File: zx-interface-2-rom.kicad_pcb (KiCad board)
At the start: 4 copper layers, 39.4 x 50.1 mm, 9 parts, among them J1 cartridge_IF2, SW1 SW_DIP_x02, U1 W27C512, U2 74LS32

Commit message: Updated SYMBOL & FOOTPRINT library
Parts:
- G200: footprint ZXINFO_LIB:ZXInfo_kicad_logo_copper_16.5x5 -> ZXINFO_FOOTPRINT:ZXInfo_kicad_logo_copper_16.5x5
- J1: footprint ZXINFO_LIB:CART_IF2_EDGE -> ZXINFO_FOOTPRINT:CART_IF2_EDGE; moved to F.Cu
- moved U1 36.5 mm to (87.1, 80.7), turned to 90 degrees
- moved J1 31.7 mm to (79.5, 90.4), turned to 0 degrees
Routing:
- net +5V: track 95.1 -> 0.00 mm
- net Net-(J1-A15): track 51.0 -> 0.00 mm
- net Net-(U1-A15): track 42.9 -> 0.00 mm
- net Net-(J1-~{MREQ}): track 41.8 -> 0.00 mm
- net Net-(J1-A14): track 37.8 -> 0.00 mm
- net Net-(U1-A14): track 37.0 -> 0.00 mm
- net A4: track 29.1 -> 0.00 mm, vias 1 -> 0
- net A5: track 29.0 -> 0.00 mm, vias 1 -> 0
- net A0: track 28.8 -> 0.00 mm, vias 1 -> 0
- net A1: track 28.8 -> 0.00 mm, vias 1 -> 0
- net A3: track 28.3 -> 0.00 mm, vias 1 -> 0
- net A2: track 28.0 -> 0.00 mm, vias 1 -> 0
- net D1: track 27.6 -> 0.00 mm
- net D2: track 27.6 -> 0.00 mm
- net D0: track 27.6 -> 0.00 mm
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- removed copper zone on B.Cu, net GND

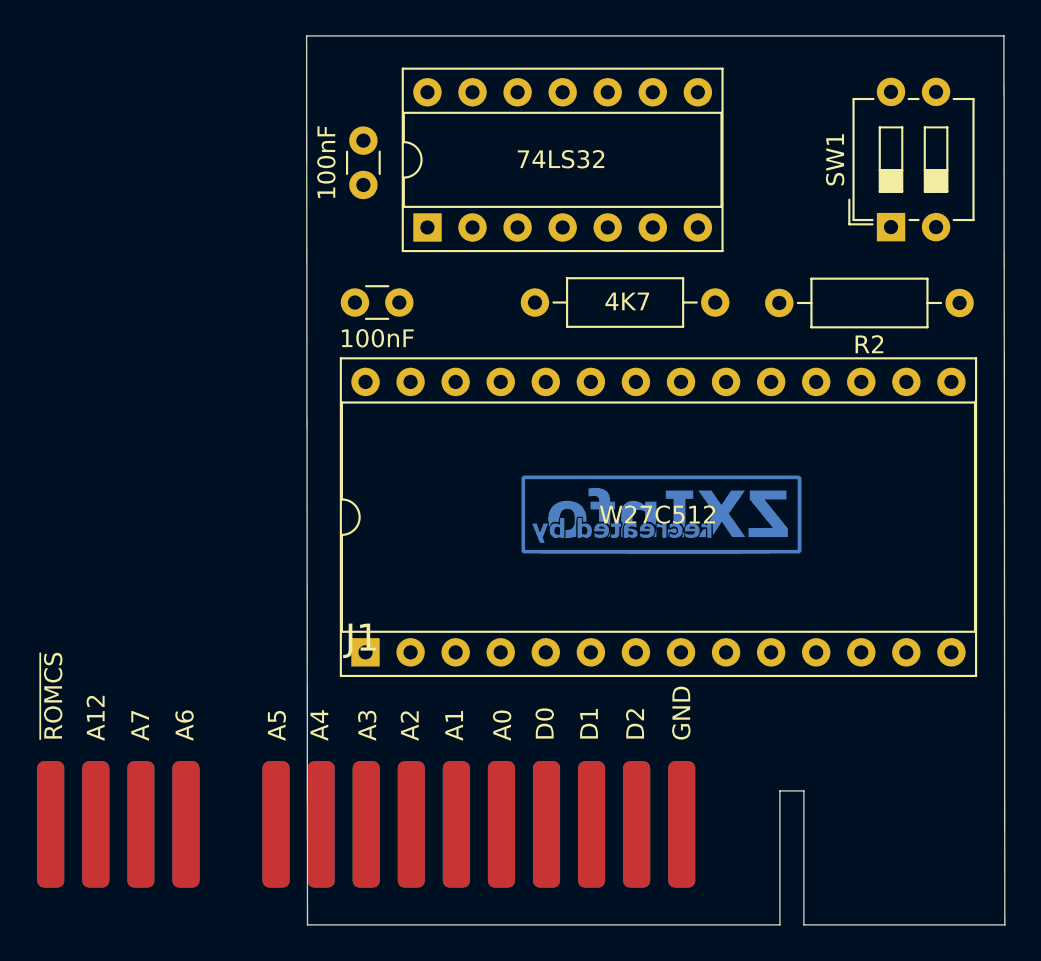
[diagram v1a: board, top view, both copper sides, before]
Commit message: version 2 - added solder mask to pad
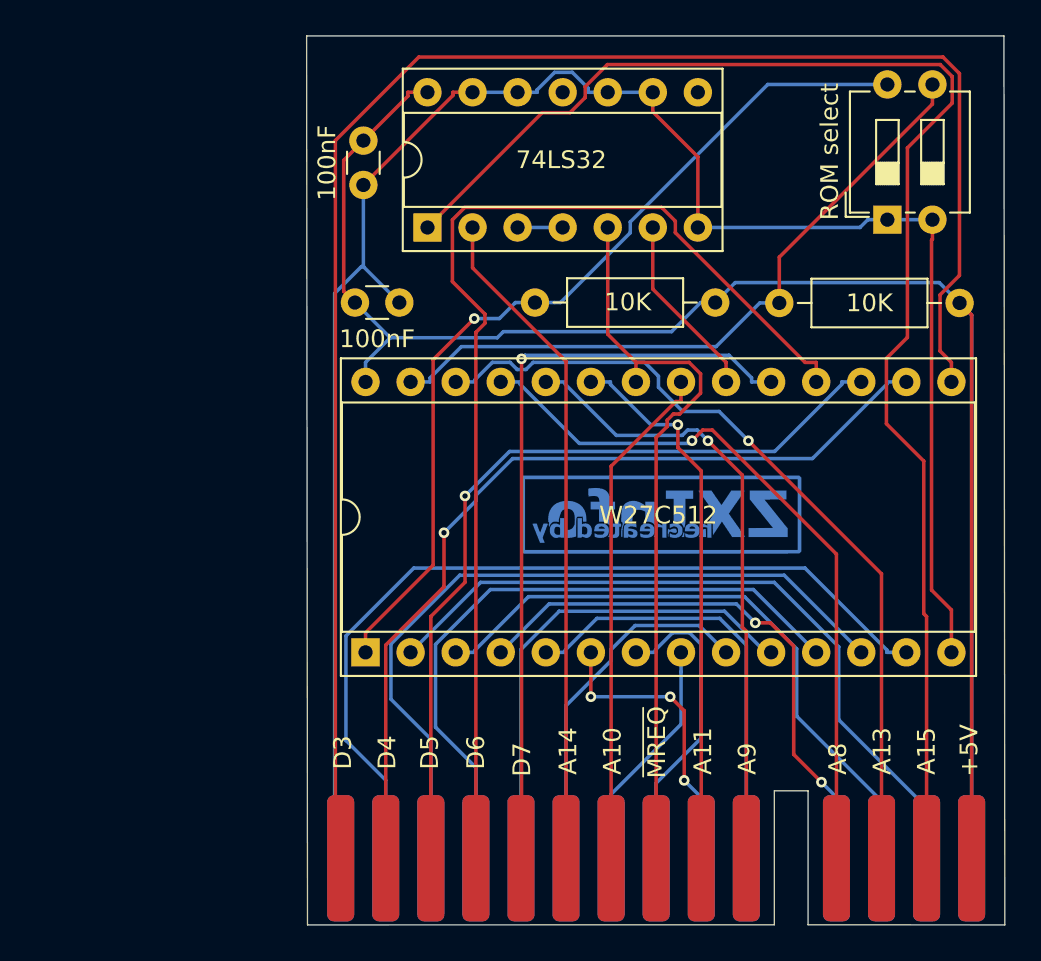
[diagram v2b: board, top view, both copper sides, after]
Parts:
- J1: moved to B.Cu
- R1, R2: value 4K7 -> 10K
- SW1: value SW_DIP_x02 -> ROM select
- moved J1 31.6 mm to (111.1, 92.3), turned to 180 degrees
- moved SW1 0.47 mm to (116.5, 56.3)
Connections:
- SW1 pad 3: Net-(U1-A15) -> Net-(U1-A14)
- SW1 pad 4: Net-(U1-A14) -> Net-(U1-A15)
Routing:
- net +5V: track 0.00 -> 117.6 mm
- net GND: track 0.00 -> 108.4 mm
- net D3: track 0.00 -> 96.2 mm
- net Net-(J1-A15): track 0.00 -> 80.5 mm
- net D6: track 0.00 -> 62.8 mm
- net Net-(U1-A15): track 0.00 -> 50.5 mm, vias 0 -> 1
- net D4: track 0.00 -> 49.5 mm, vias 0 -> 1
- net D2: track 0.00 -> 48.7 mm
- net D5: track 0.00 -> 46.3 mm, vias 0 -> 1
- net A13: track 0.00 -> 46.2 mm, vias 0 -> 1
- net D7: track 0.00 -> 43.1 mm, vias 0 -> 1
- net D1: track 0.00 -> 42.9 mm
- net Net-(J1-~{MREQ}): track 0.00 -> 41.8 mm
- net A12: track 0.00 -> 41.2 mm
- net A8: track 0.00 -> 40.8 mm, vias 0 -> 1
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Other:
- outline, holes or cut-outs redrawn
- copper layers 4 -> 2
